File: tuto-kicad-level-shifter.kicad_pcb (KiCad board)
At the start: 2 copper layers, 14 parts, among them J1 Conn_01x01_Pin, J2 Conn_01x01_Pin, J3 Conn_01x01_Pin, J4 Conn_01x01_Pin, J5 Conn_01x01_Pin, J6 Conn_01x01_Pin, J7 Conn_01x01_Pin, U1 PCA9306

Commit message: Placement des composants et contour
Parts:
- moved R1 133.9 mm to (134.2, 87.4)
- moved C1 133.9 mm to (134.2, 85.8), turned to 180 degrees
- moved R5 132.1 mm to (137.7, 81.3)
- moved U1 130.8 mm to (138.4, 87.2), turned to 90 degrees
- moved R2 128.0 mm to (140.1, 91.4)
- moved J2 127.4 mm to (132.1, 81.3)
- moved J1 127.1 mm to (132.1, 94.0)
- moved J7 126.5 mm to (137.2, 94.0)
- moved R4 124.6 mm to (144.4, 85.1), turned to 180 degrees
- moved R3 123.2 mm to (145.0, 91.1)
- moved J4 118.4 mm to (142.2, 81.3)
- moved J6 116.8 mm to (147.3, 81.3)
- moved J3 116.8 mm to (142.2, 94.0)
- moved J5 116.5 mm to (147.3, 94.0)
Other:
- board outline added: 20.3 x 17.8 mm

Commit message: Routage
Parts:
- moved R4 7.90 mm to (137.4, 81.3), turned to 0 degrees
- moved R5 7.83 mm to (144.6, 85.1), turned to 180 degrees
- moved U1 0.20 mm to (138.4, 87.0)
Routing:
- net VDD2: track 0.00 -> 28.5 mm, vias 0 -> 2
- net VDD1: track 0.00 -> 18.5 mm, vias 0 -> 2
- net Net-(J5-Pin_1): track 0.00 -> 12.0 mm
- net Net-(J6-Pin_1): track 0.00 -> 11.2 mm
- net /VREF2: track 0.00 -> 8.69 mm
- net Net-(J4-Pin_1): track 0.00 -> 8.13 mm
- net Net-(J3-Pin_1): track 0.00 -> 7.62 mm
- net GND: track 0.00 -> 4.03 mm, vias 0 -> 2
- added copper zone on B.Cu, net GND

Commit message: Annotations
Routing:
- net GND: track 4.03 -> 4.83 mm
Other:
- board text added: "GND"
- board text added: "Level Shifter I2C"
- board text added: "SCL1"
- board text added: "SCL2"
- board text added: "SDA1"
- board text added: "SDA2"
- board text added: "V1.0"
- board text added: "VDD1<VDD2"
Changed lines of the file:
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@@
 			(at 0 -2.33 0)
 			(layer "F.SilkS")
+			(hide yes)
 			(effects
 				(font
@@
 			(at 0 2.33 0)
 			(layer "F.Fab")
+			(hide yes)
 			(effects
 				(font
@@
 			(at 0 -2.33 0)
 			(layer "F.SilkS")
+			(hide yes)
 			(effects
 				(font
@@
 			(at 0 2.33 0)
 			(layer "F.Fab")
+			(hide yes)
 			(effects
 				(font
@@
 		(tags "resistor")
 		(property "Reference" "R1"
-			(at 0 -1.43 0)
+			(at 0.1 1.7 0)
 			(layer "F.SilkS")
 			(effects
@@
 		)
 		(property "Value" "NA"
-			(at 0 1.43 0)
+			(at -0.275 1.4 0)
 			(layer "F.Fab")
 			(effects
@@
 			(at 0 -2.33 0)
 			(layer "F.SilkS")
+			(hide yes)
 			(effects
 				(font
@@
 			(at 0 2.33 0)
 			(layer "F.Fab")
+			(hide yes)
 			(effects
 				(font
@@
 			(at 0 -2.33 0)
 			(layer "F.SilkS")
+			(hide yes)
 			(effects
 				(font
@@
 			(at 0 2.33 0)
 			(layer "F.Fab")
+			(hide yes)
 			(effects
 				(font
@@
 			(at 0 -2.33 0)
 			(layer "F.SilkS")
+			(hide yes)
 			(effects
 				(font
@@
 			(at 0 2.33 0)
 			(layer "F.Fab")
+			(hide yes)
 			(effects
 				(font
@@
 			(at 0 -2.33 0)
 			(layer "F.SilkS")
+			(hide yes)
 			(effects
 				(font
@@
 			(at 0 2.33 0)
 			(layer "F.Fab")
+			(hide yes)
 			(effects
 				(font
@@
 		(tags "capacitor")
 		(property "Reference" "C1"
-			(at 0 -1.43 180)
+			(at -0.1 1.6 180)
 			(layer "F.SilkS")
 			(effects
@@
 		(tags "resistor")
 		(property "Reference" "R5"
-			(at 0 -1.43 180)
+			(at 0 -1.5 180)
 			(layer "F.SilkS")
 			(effects
@@
 		(tags "resistor")
 		(property "Reference" "R3"
-			(at 0 -1.43 0)
+			(at 0 -1.6 0)
 			(layer "F.SilkS")
 			(effects
@@
 		(tags "SSOP-8 2.95x2.8mm Pitch 0.65mm")
 		(property "Reference" "U1"
-			(at 0 -2.4 -90)
+			(at -0.205 2.7 0)
 			(layer "F.SilkS")
 			(effects
@@
 		)
 		(property "Value" "PCA9306"
-			(at 0 2.6 -90)
+			(at -2.405 1.4 0)
 			(layer "F.Fab")
 			(effects
@@
 			(at 0 -2.33 0)
 			(layer "F.SilkS")
+			(hide yes)
 			(effects
 				(font
@@
 			(at 0 2.33 0)
 			(layer "F.Fab")
+			(hide yes)
 			(effects
 				(font
@@
 		(layer "Edge.Cuts")
 	)
+	(gr_text "Level Shifter I2C"
+		(at 147.2 87.2 0)
+		(layer "B.SilkS")
+		(effects
+			(font
+				(size 1.2 1.2)
+				(thickness 0.18)
+			)
+			(justify left bottom mirror)
+		)
+	)
+	(gr_text "V1.0"
+		(at 147.1 89.3 0)
+		(layer "B.SilkS")
+		(effects
+			(font
+				(size 1.2 1.2)
+				(thickness 0.18)
+			)
+			(justify left bottom mirror)
+		)
+	)
+	(gr_text "SCL2"
+		(at 142.7 86.6 90)
+		(layer "F.SilkS")
+		(effects
+			(font
+				(size 1 1)
+				(thickness 0.15)
+			)
+			(justify left bottom)
+		)
+	)
+	(gr_text "SDA1"
+		(at 148 92.3 90)
+		(layer "F.SilkS")
+		(effects
+			(font
+				(size 1 1)
+				(thickness 0.15)
+			)
+			(justify left bottom)
+		)
+	)
+	(gr_text "SCL1"
+		(at 142.6 92.3 90)
+		(layer "F.SilkS")
+		(effects
+			(font
+				(size 1 1)
+				(thickness 0.15)
+			)
+			(justify left bottom)
+		)
+	)
+	(gr_text "SDA2"
+		(at 148.1 86.7 90)
+		(layer "F.SilkS")
+		(effects
+			(font
+				(size 1 1)
+				(thickness 0.15)
+			)
+			(justify left bottom)
+		)
+	)
+	(gr_text "GND"
+		(at 137.7 92.5 90)
+		(layer "F.SilkS")
+		(effects
+			(font
+				(size 1 1)
+				(thickness 0.15)
+			)
+			(justify left bottom)
+		)
+	)
+	(gr_text "VDD1<VDD2"
+		(at 132.5 92 90)
+		(layer "F.SilkS")
+		(effects
+			(font
+				(size 1 1)
+				(thickness 0.15)
+			)
+			(justify left bottom)
+		)
+	)
 	(segment
 		(start 133.425 85.8)
@@
 	)
 	(segment
-		(start 137.425 89.575)
+		(start 135.2 90.3)
 		(end 136.7 90.3)
 		(width 0.25)
@@
 	)
 	(segment
-		(start 137.425 88.695)
-		(end 137.425 89.575)
+		(start 137.425 89.575)
+		(end 137.425 88.695)
 		(width 0.25)
 		(layer "F.Cu")
@@
 	(segment
 		(start 136.7 90.3)
-		(end 136 90.3)
+		(end 137.425 89.575)
 		(width 0.25)
 		(layer "F.Cu")
@@
 	)
 	(via
-		(at 136 90.3)
+		(at 135.2 90.3)
 		(size 0.6)
 		(drill 0.3)
@@
 	)
 	(segment
-		(start 133.6 91.4)
-		(end 137.6 91.4)
-		(width 0.25)
-		(layer "F.Cu")
-		(net 3)
-	)
-	(segment
 		(start 132.08 92.92)
-		(end 133.6 91.4)
+		(end 132.08 93.98)
 		(width 0.25)
 		(layer "F.Cu")
@@
 	)
 	(segment
-		(start 142.9 91.2)
-		(end 144.075 91.2)
+		(start 138.3 91.4)
+		(end 138.075 91.175)
 		(width 0.25)
 		(layer "F.Cu")
@@
 	)
 	(segment
-		(start 137.6 90.25)
-		(end 137.6 91.4)
+		(start 138.075 91.175)
+		(end 138.075 88.695)
 		(width 0.25)
 		(layer "F.Cu")
@@
 	)
 	(segment
-		(start 137.6 91.4)
-		(end 139.25 91.4)
+		(start 143.5 91.1)
+		(end 144.175 91.1)
 		(width 0.25)
 		(layer "F.Cu")
@@
 	)
 	(segment
-		(start 144.075 91.2)
-		(end 144.175 91.1)
+		(start 143.1 90.7)
+		(end 143.5 91.1)
 		(width 0.25)
 		(layer "F.Cu")
@@
 	)
 	(segment
-		(start 138.075 89.775)
-		(end 137.6 90.25)
+		(start 138.3 91.4)
+		(end 133.6 91.4)
 		(width 0.25)
 		(layer "F.Cu")
@@
 	)
 	(segment
-		(start 138.075 88.695)
-		(end 138.075 89.775)
+		(start 138.3 91.4)
+		(end 139.25 91.4)
 		(width 0.25)
 		(layer "F.Cu")
@@
 	)
 	(segment
-		(start 132.08 92.92)
-		(end 132.08 93.98)
+		(start 133.6 91.4)
+		(end 132.08 92.92)
 		(width 0.25)
 		(layer "F.Cu")
@@
 	)
 	(via
-		(at 142.9 91.2)
+		(at 143.1 90.7)
 		(size 0.6)
 		(drill 0.3)
@@
 	)
 	(via
-		(at 137.6 91.4)
+		(at 138.3 91.4)
 		(size 0.6)
 		(drill 0.3)
@@
 	)
 	(segment
-		(start 142.7 91.4)
-		(end 142.9 91.2)
+		(start 142.4 91.4)
+		(end 138.3 91.4)
 		(width 0.25)
 		(layer "B.Cu")
@@
 	)
 	(segment
-		(start 137.6 91.4)
-		(end 142.7 91.4)
+		(start 143.1 90.7)
+		(end 142.4 91.4)
 		(width 0.25)
 		(layer "B.Cu")

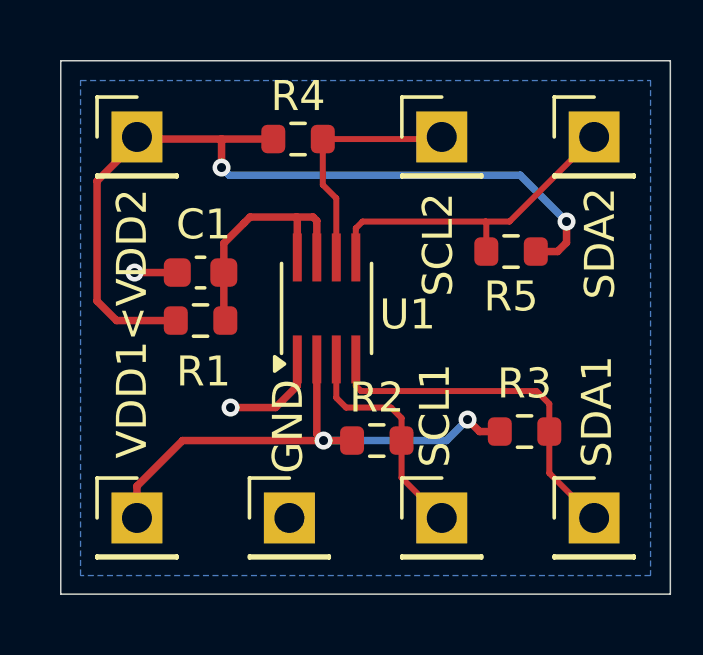
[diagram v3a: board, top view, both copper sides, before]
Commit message: Corrections après DRC
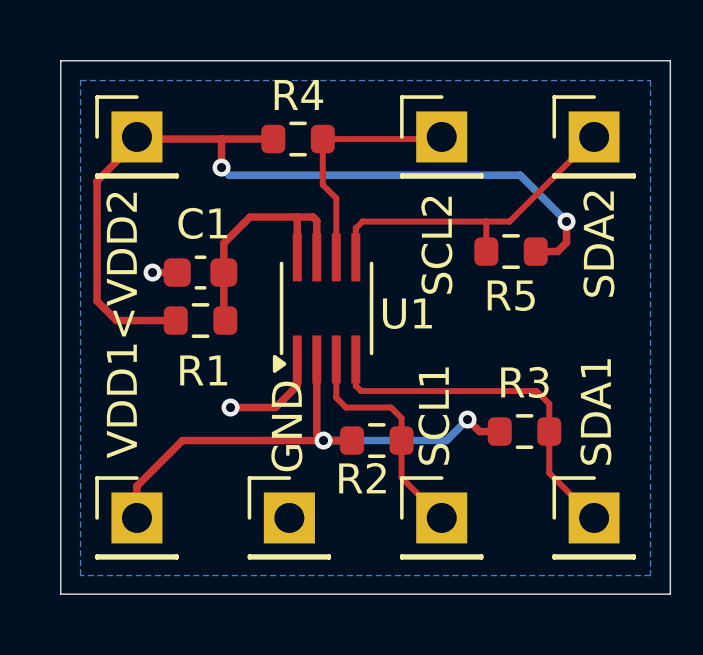
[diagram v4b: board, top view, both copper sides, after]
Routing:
- net GND: track 4.83 -> 4.23 mm
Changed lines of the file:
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@@
 		(tags "resistor")
 		(property "Reference" "R2"
-			(at 0 -1.43 0)
+			(at -0.475 1.3 0)
 			(layer "F.SilkS")
 			(effects
@@
 	)
 	(gr_text "Level Shifter I2C"
-		(at 147.2 87.2 0)
+		(at 147.2 87.9 0)
 		(layer "B.SilkS")
 		(effects
@@
 	)
 	(gr_text "V1.0"
-		(at 147.1 89.3 0)
+		(at 147.1 89.7 0)
 		(layer "B.SilkS")
 		(effects
@@
 	)
 	(gr_text "VDD1<VDD2"
-		(at 132.5 92 90)
+		(at 132.2 92 90)
 		(layer "F.SilkS")
 		(effects
@@
 			(justify left bottom)
 		)
-	)
-	(segment
-		(start 133.425 85.8)
-		(end 132 85.8)
-		(width 0.25)
-		(layer "F.Cu")
-		(net 1)
 	)
 	(segment
@@
 		(start 137.425 89.575)
 		(end 137.425 88.695)
+		(width 0.25)
+		(layer "F.Cu")
+		(net 1)
+	)
+	(segment
+		(start 133.425 85.8)
+		(end 132.6 85.8)
 		(width 0.25)
 		(layer "F.Cu")
@@
 	)
 	(via
-		(at 132 85.8)
+		(at 132.6 85.8)
 		(size 0.6)
 		(drill 0.3)
